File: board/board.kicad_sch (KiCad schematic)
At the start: 0 parts

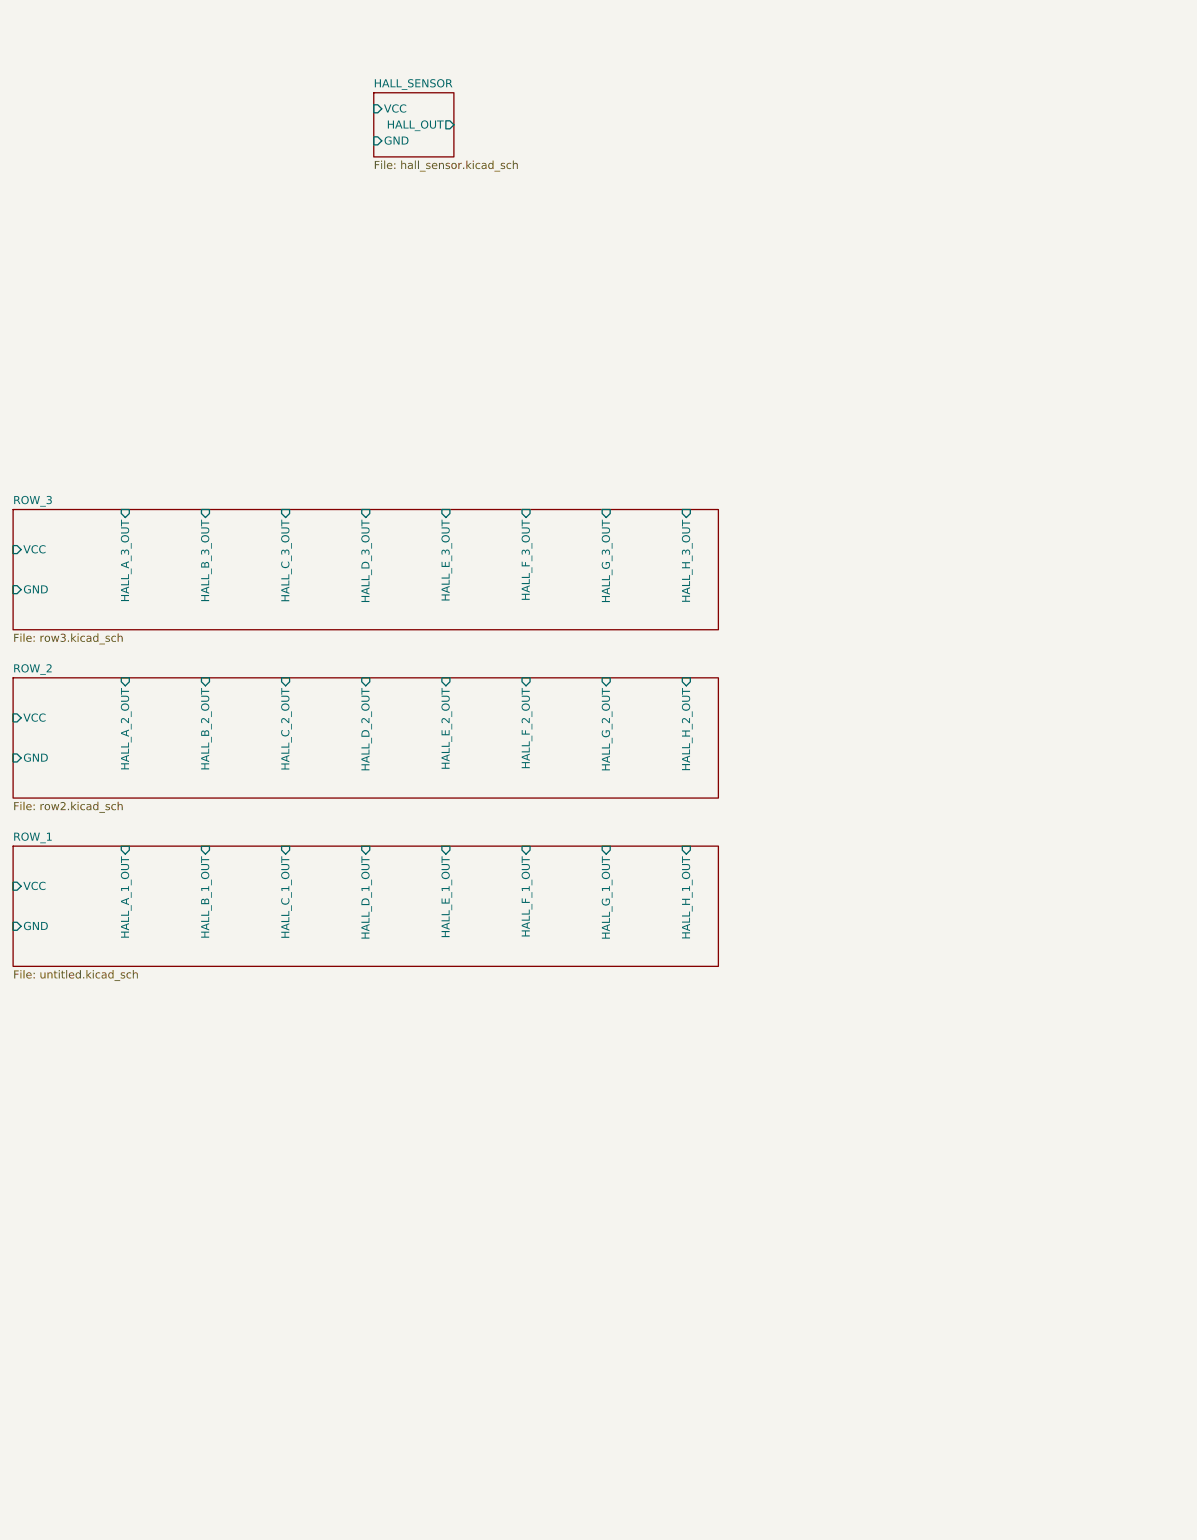
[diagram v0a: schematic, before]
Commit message: Connected all rows to MCPs
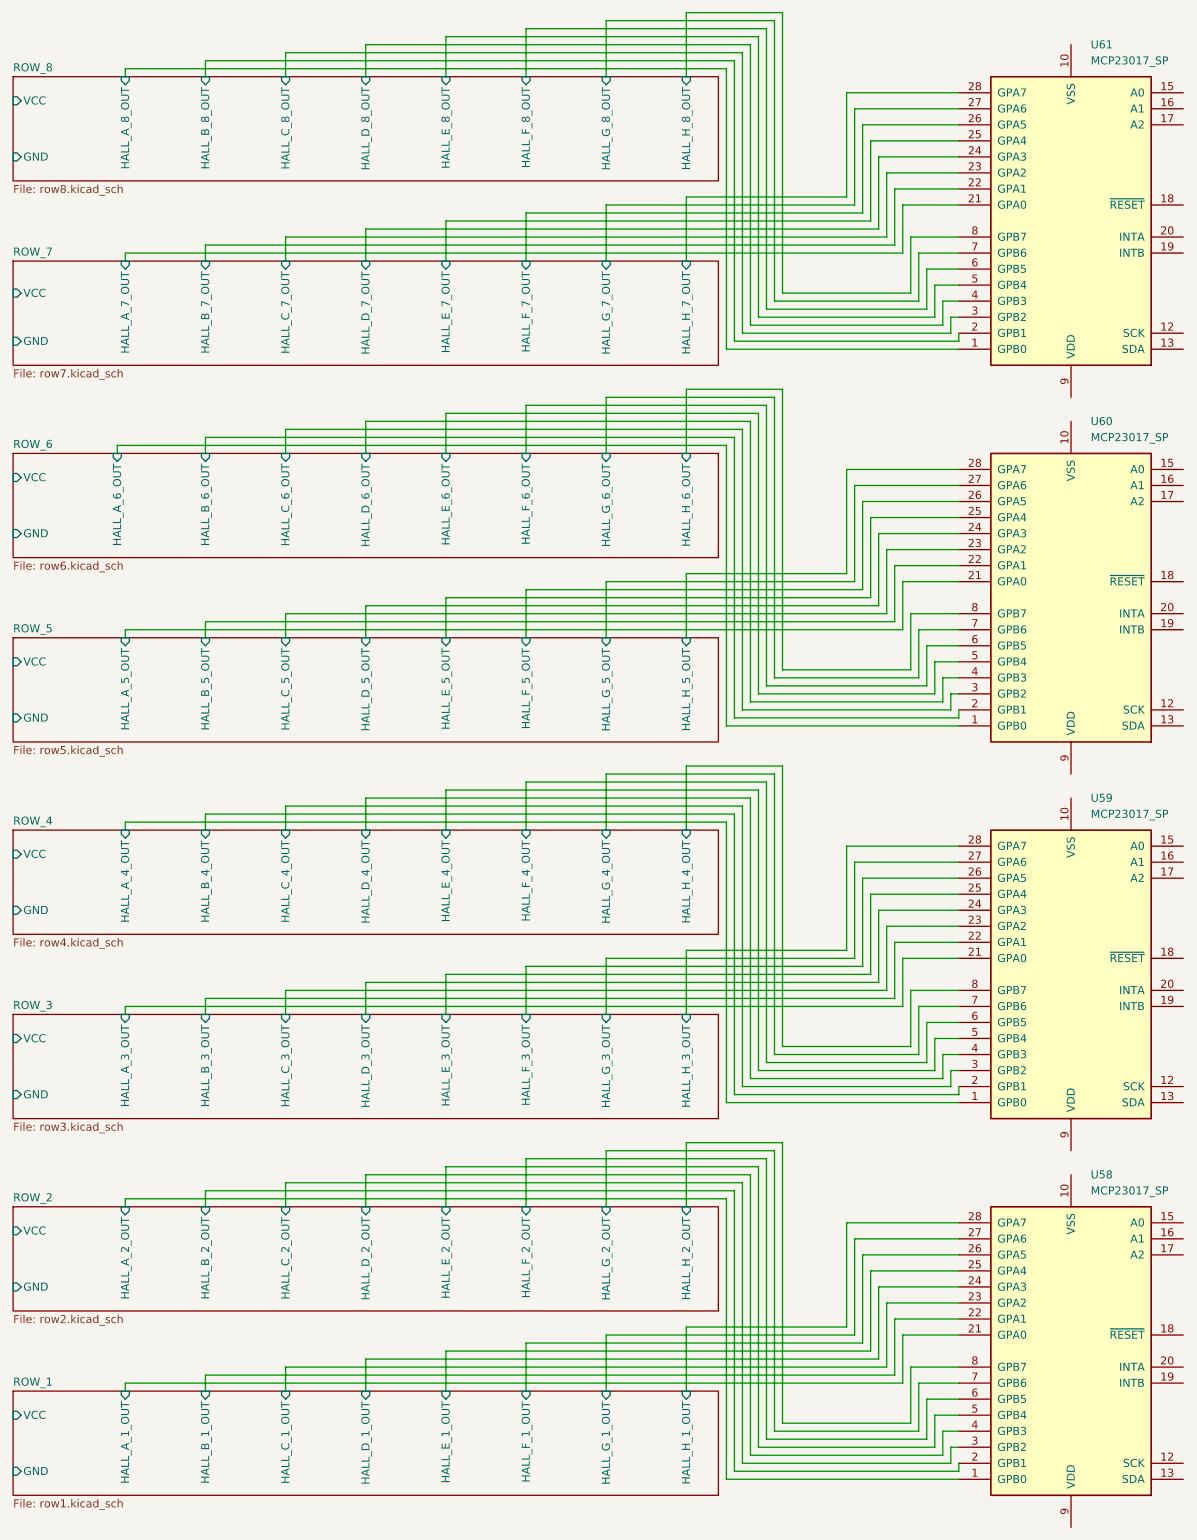
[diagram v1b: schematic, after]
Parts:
- added U58, U59, U60, U61: MCP23017_SP, Package_DIP:DIP-28_W7.62mm, symbol Interface_Expansion:MCP23017_SP
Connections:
- net ROW_1/HALL_A_1_OUT: now also U58.21 (GPA0)
- net ROW_1/HALL_B_1_OUT: now also U58.22 (GPA1)
- net ROW_1/HALL_C_1_OUT: now also U58.23 (GPA2)
- net ROW_1/HALL_D_1_OUT: now also U58.24 (GPA3)
- net ROW_1/HALL_E_1_OUT: now also U58.25 (GPA4)
- net ROW_1/HALL_F_1_OUT: now also U58.26 (GPA5)
- net ROW_1/HALL_G_1_OUT: now also U58.27 (GPA6)
- net ROW_1/HALL_H_1_OUT: now also U58.28 (GPA7)
- net ROW_2/HALL_A_2_OUT: now also U58.1 (GPB0)
- net ROW_2/HALL_B_2_OUT: now also U58.2 (GPB1)
- net ROW_2/HALL_C_2_OUT: now also U58.3 (GPB2)
- net ROW_2/HALL_D_2_OUT: now also U58.4 (GPB3)
- net ROW_2/HALL_E_2_OUT: now also U58.5 (GPB4)
- net ROW_2/HALL_F_2_OUT: now also U58.6 (GPB5)
- net ROW_2/HALL_G_2_OUT: now also U58.7 (GPB6)
- net ROW_2/HALL_H_2_OUT: now also U58.8 (GPB7)
- net ROW_3/HALL_A_3_OUT: now also U59.21 (GPA0)
- net ROW_3/HALL_B_3_OUT: now also U59.22 (GPA1)
- net ROW_3/HALL_C_3_OUT: now also U59.23 (GPA2)
- net ROW_3/HALL_D_3_OUT: now also U59.24 (GPA3)
- net ROW_3/HALL_E_3_OUT: now also U59.25 (GPA4)
- net ROW_3/HALL_F_3_OUT: now also U59.26 (GPA5)
- net ROW_3/HALL_G_3_OUT: now also U59.27 (GPA6)
- net ROW_3/HALL_H_3_OUT: now also U59.28 (GPA7)
- new net ROW_4/HALL_A_4_OUT: U59.1 (GPB0)
- new net ROW_4/HALL_B_4_OUT: U59.2 (GPB1)
- new net ROW_4/HALL_C_4_OUT: U59.3 (GPB2)
- new net ROW_4/HALL_D_4_OUT: U59.4 (GPB3)
- new net ROW_4/HALL_E_4_OUT: U59.5 (GPB4)
- new net ROW_4/HALL_F_4_OUT: U59.6 (GPB5)
- new net ROW_4/HALL_G_4_OUT: U59.7 (GPB6)
- new net ROW_4/HALL_H_4_OUT: U59.8 (GPB7)
- new net ROW_5/HALL_A_5_OUT: U60.21 (GPA0)
- new net ROW_5/HALL_B_5_OUT: U60.22 (GPA1)
- new net ROW_5/HALL_C_5_OUT: U60.23 (GPA2)
- new net ROW_5/HALL_D_5_OUT: U60.24 (GPA3)
- new net ROW_5/HALL_E_5_OUT: U60.25 (GPA4)
- new net ROW_5/HALL_F_5_OUT: U60.26 (GPA5)
- new net ROW_5/HALL_G_5_OUT: U60.27 (GPA6)
- new net ROW_5/HALL_H_5_OUT: U60.28 (GPA7)
- new net ROW_6/HALL_A_6_OUT: U60.1 (GPB0)
- new net ROW_6/HALL_B_6_OUT: U60.2 (GPB1)
- new net ROW_6/HALL_C_6_OUT: U60.3 (GPB2)
- new net ROW_6/HALL_D_6_OUT: U60.4 (GPB3)
- new net ROW_6/HALL_E_6_OUT: U60.5 (GPB4)
- new net ROW_6/HALL_F_6_OUT: U60.6 (GPB5)
- new net ROW_6/HALL_G_6_OUT: U60.7 (GPB6)
- new net ROW_6/HALL_H_6_OUT: U60.8 (GPB7)
- new net ROW_7/HALL_A_7_OUT: U61.21 (GPA0)
- new net ROW_7/HALL_B_7_OUT: U61.22 (GPA1)
- new net ROW_7/HALL_C_7_OUT: U61.23 (GPA2)
- new net ROW_7/HALL_D_7_OUT: U61.24 (GPA3)
- new net ROW_7/HALL_E_7_OUT: U61.25 (GPA4)
- new net ROW_7/HALL_F_7_OUT: U61.26 (GPA5)
- new net ROW_7/HALL_G_7_OUT: U61.27 (GPA6)
- new net ROW_7/HALL_H_7_OUT: U61.28 (GPA7)
- new net ROW_8/HALL_A_8_OUT: U61.1 (GPB0)
- new net ROW_8/HALL_B_8_OUT: U61.2 (GPB1)
- new net ROW_8/HALL_C_8_OUT: U61.3 (GPB2)
- new net ROW_8/HALL_D_8_OUT: U61.4 (GPB3)
- new net ROW_8/HALL_E_8_OUT: U61.5 (GPB4)
- new net ROW_8/HALL_F_8_OUT: U61.6 (GPB5)
- new net ROW_8/HALL_G_8_OUT: U61.7 (GPB6)
- new net ROW_8/HALL_H_8_OUT: U61.8 (GPB7)
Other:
- removed sheet HALL_SENSOR
- added sheet ROW_4 (row4.kicad_sch)
- added sheet ROW_5 (row5.kicad_sch)
- added sheet ROW_6 (row6.kicad_sch)
- added sheet ROW_7 (row7.kicad_sch)
- added sheet ROW_8 (row8.kicad_sch)
- sheet ROW_1: file untitled.kicad_sch -> row1.kicad_sch

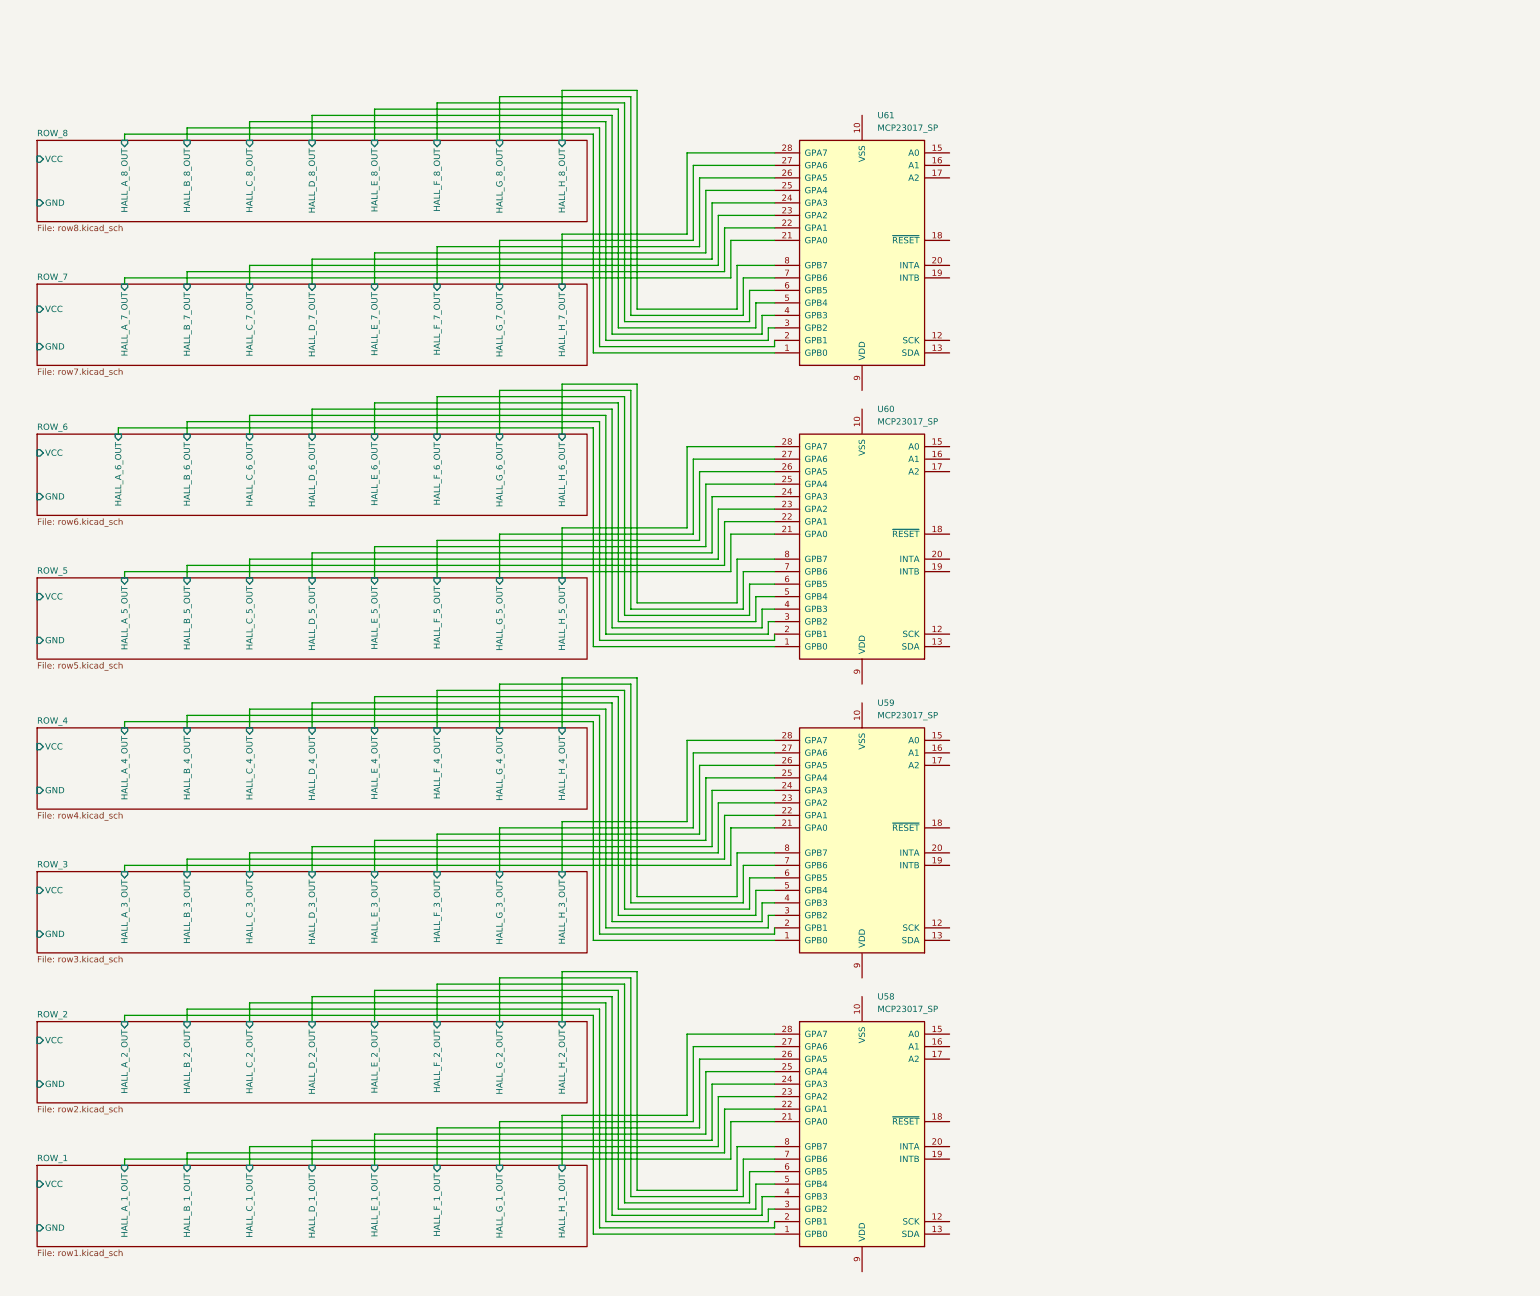
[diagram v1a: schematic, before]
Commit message: connected all sensors to mcps and all mcps to rpi4
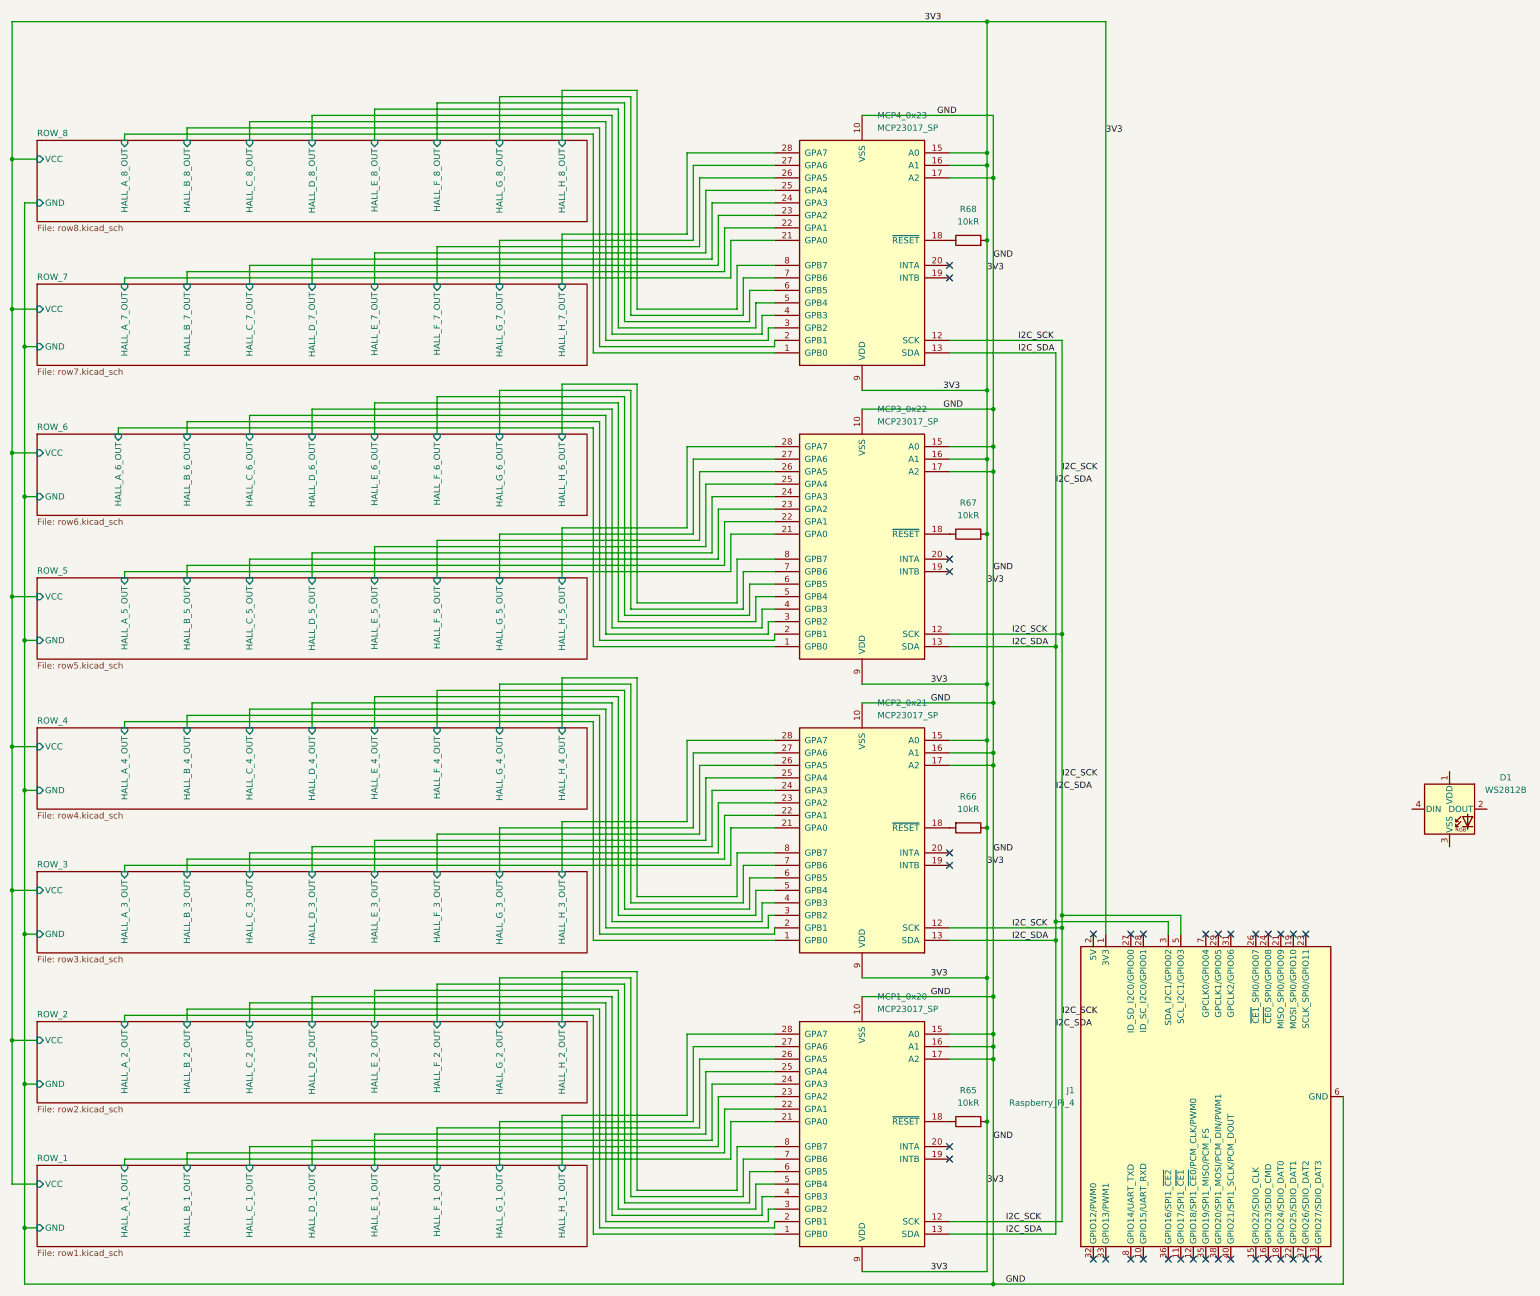
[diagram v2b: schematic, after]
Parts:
- added D1: WS2812B, LED_SMD:LED_WS2812B_PLCC4_5.0x5.0mm_P3.2mm, symbol LED:WS2812B
- added J1: Raspberry_Pi_4, symbol Connector:Raspberry_Pi_4
- added R65, R66, R67, R68: 10kR, symbol Device:R
- renumbered U58 to MCP1_0x20, U59 to MCP2_0x21, U60 to MCP3_0x22, U61 to MCP4_0x23
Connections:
- net GND: now reaches MCP4_0x23.10 (VSS)
- net GND: now also MCP1_0x20.10 (VSS), MCP1_0x20.15 (A0), MCP1_0x20.16 (A1), MCP1_0x20.17 (A2), MCP2_0x21.10 (VSS), MCP2_0x21.16 (A1), MCP2_0x21.17 (A2), MCP3_0x22.10 (VSS), MCP3_0x22.15 (A0), MCP3_0x22.17 (A2), MCP4_0x23.17 (A2), J1.14 (GND), J1.20 (GND), J1.25 (GND), J1.30 (GND), J1.34 (GND), J1.39 (GND), J1.6 (GND), J1.9 (GND)
- net I2C_SCK: now reaches MCP4_0x23.12 (SCK)
- net I2C_SCK: now also MCP1_0x20.12 (SCK), MCP2_0x21.12 (SCK), MCP3_0x22.12 (SCK), J1.5 (SCL_I2C1/GPIO03)
- net I2C_SDA: now reaches MCP4_0x23.13 (SDA)
- net I2C_SDA: now also MCP1_0x20.13 (SDA), MCP2_0x21.13 (SDA), MCP3_0x22.13 (SDA), J1.3 (SDA_I2C1/GPIO02)
- net 3V3: now reaches MCP4_0x23.15 (A0)
- net 3V3: now also MCP1_0x20.9 (VDD), MCP2_0x21.15 (A0), MCP2_0x21.9 (VDD), MCP3_0x22.16 (A1), MCP3_0x22.9 (VDD), MCP4_0x23.16 (A1), MCP4_0x23.9 (VDD), J1.1 (3V3), J1.17 (3V3), R65.2, R66.1, R67.2, R68.2
- net at MCP4_0x23.18 (~{RESET}): now also R68.1
- net at MCP3_0x22.18 (~{RESET}): now also R67.1
- net at MCP2_0x21.18 (~{RESET}): now also R66.2
- net at MCP1_0x20.18 (~{RESET}): now also R65.1
- new net: J1.2 (5V), J1.4 (5V)
- no-connect marks 0 -> 35
